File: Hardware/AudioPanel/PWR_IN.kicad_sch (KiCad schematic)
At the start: 30 parts, among them Q5 Q_PMOS, U17 LM358, U40 LM1084-ADJ, U41 NE5534

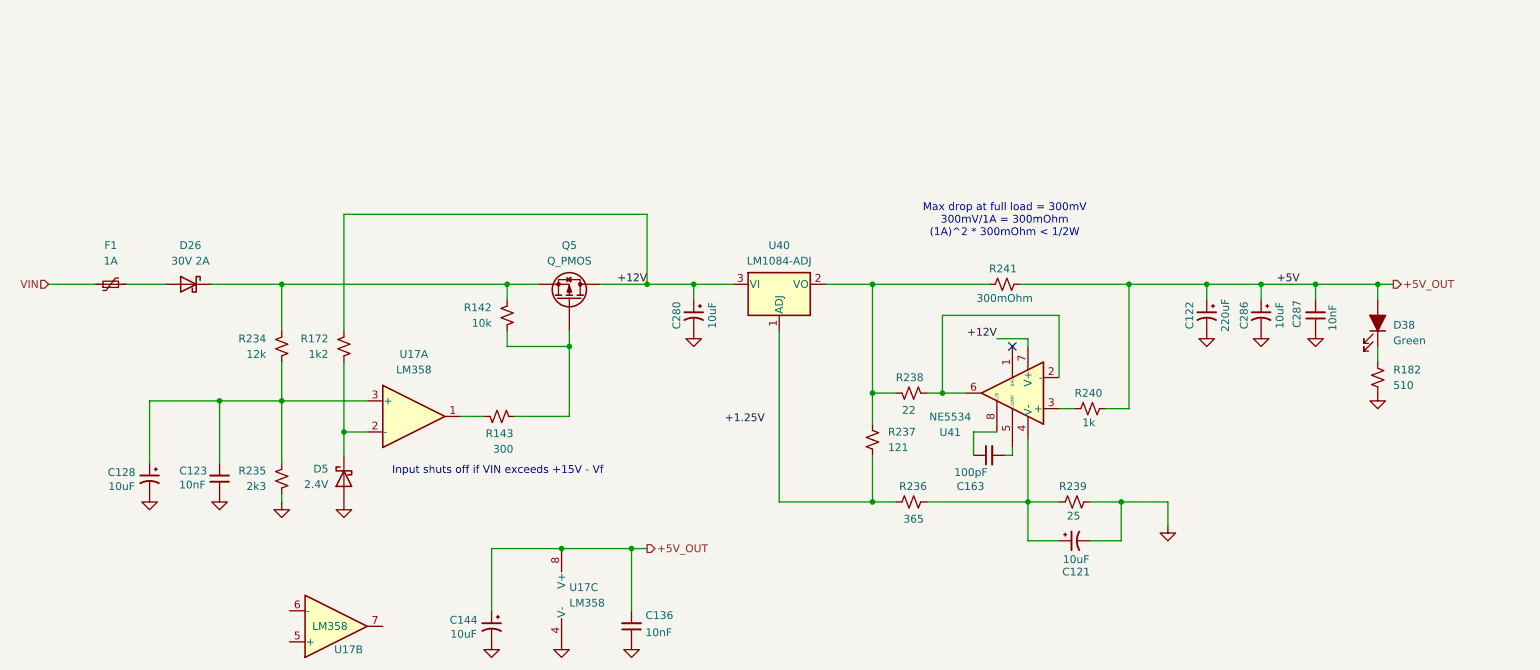
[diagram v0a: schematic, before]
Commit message: Added ideal diode controller to main power input
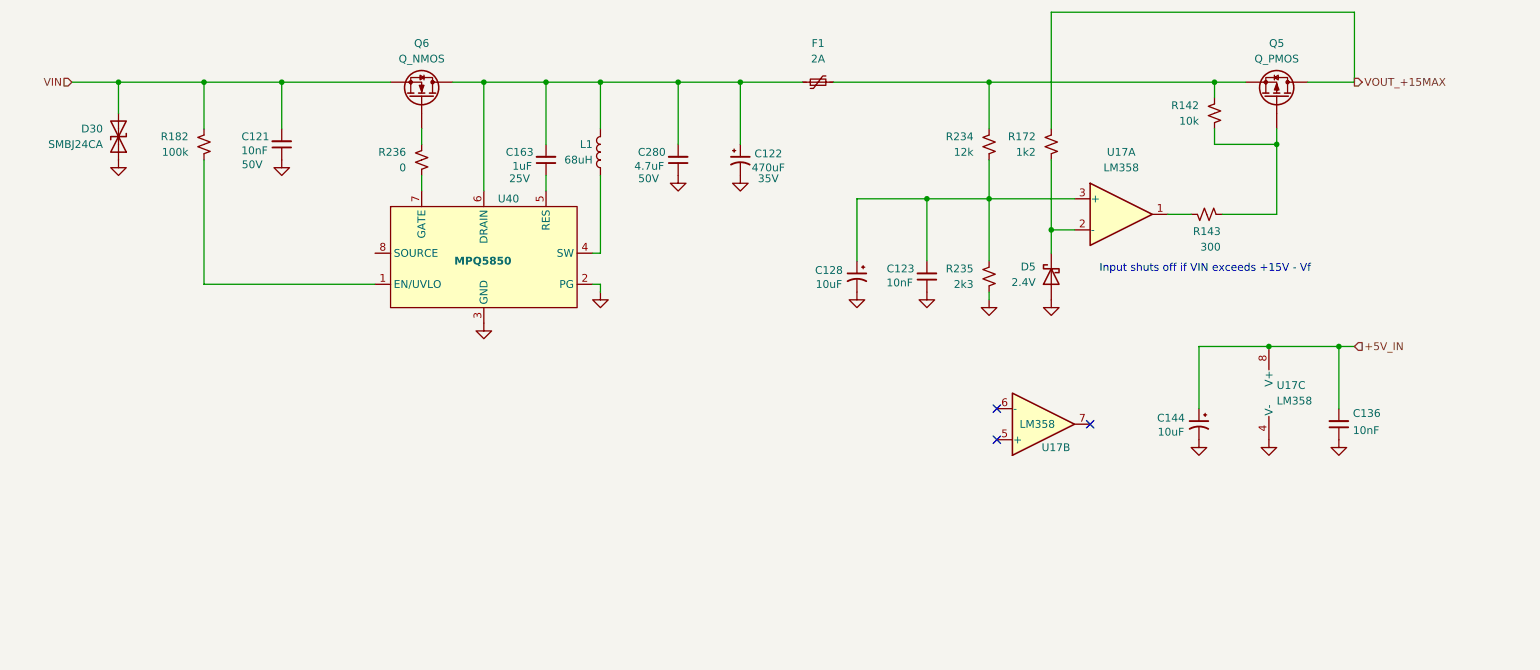
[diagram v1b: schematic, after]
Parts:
- removed C121, C280, C286: 10uF, symbol Device:C_Polarized_Small_US
- removed C287: 10nF, symbol Device:C_Small
- removed D26: 30V 2A, symbol Device:D_Schottky
- removed D38: Green, LED_THT:LED_D5.0mm, symbol Device:LED_Filled
- removed R237: 121, Resistor_SMD:R_0603_1608Metric_Pad0.98x0.95mm_HandSolder, symbol Device:R_Small_US
- removed R238: 22, Resistor_SMD:R_0603_1608Metric_Pad0.98x0.95mm_HandSolder, symbol Device:R_Small_US
- removed R239: 25, Resistor_SMD:R_0603_1608Metric_Pad0.98x0.95mm_HandSolder, symbol Device:R_Small_US
- removed R240: 1k, Resistor_SMD:R_0603_1608Metric_Pad0.98x0.95mm_HandSolder, symbol Device:R_Small_US
- removed R241: 300mOhm, Resistor_SMD:R_0603_1608Metric_Pad0.98x0.95mm_HandSolder, symbol Device:R_Small_US
- removed U40: LM1084-ADJ, symbol Regulator_Linear:LM1084-ADJ
- removed U41: NE5534, symbol Amplifier_Operational:NE5534
- added C121: 10nF, Capacitor_SMD:C_0603_1608Metric, symbol Device:C_Small
- added C280: 4.7uF, symbol Device:C_Small
- added D30: SMBJ24CA, symbol Device:D_TVS
- added L1: 68uH, symbol Device:L
- added Q6: Q_NMOS, symbol Device:Q_NMOS
- added U40: MPQ5850, Package_TO_SOT_SMD:TSOT-23-8, symbol AudioPanelLibrary:MPQ5850
- C122: value 220uF -> 470uF; Voltage (none) -> 35V
- C163: value 100pF -> 1uF; footprint (none) -> Capacitor_SMD:C_0805_2012Metric; Voltage (none) -> 25V
- F1: value 1A -> 2A
- R182: value 510 -> 100k
- R236: value 365 -> 0
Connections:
- net GND: now also C121.1, C280.1, D30.1 (A1), U40.2 (PG), U40.3 (GND); no longer R182.1
- net VIN: now also R182.2, C121.2, D30.2 (A2), Q6.S; no longer F1.1
- net at Q5.S, R142.2, R234.2: now also F1.2
- net at R236.1: now also U40.7 (GATE)
- net at R236.2: now also Q6.G
- net at C163.1: now also U40.5 (RES)
- net at C163.2: now also C122.1, F1.1, C280.2, L1.1, Q6.D, U40.6 (DRAIN)
- net +12V renamed VOUT_+15MAX
- net +5V_OUT renamed +5V_IN
- net +5V_IN: no longer C122.1
- new net: L1.2, U40.4 (SW)
- new net: R182.1, U40.1 (EN/UVLO)
- no-connect marks 1 -> 3
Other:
- note removed: "Max drop at full load = 300mV 300mV/1A = 300mOhm (1A)^2 * 300mOhm < 1/2W"
- moved on the sheet: C123, C128, C136, C144, D5, F1, Q5, R142, R143, R172, R234, R235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

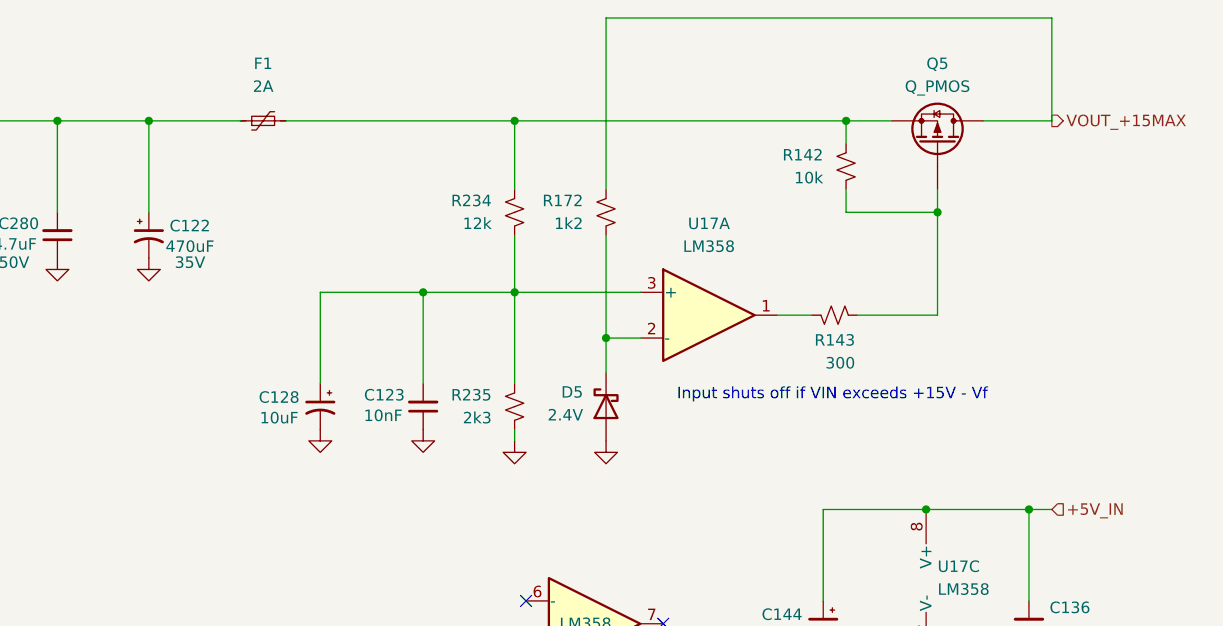
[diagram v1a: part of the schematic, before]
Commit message: Adding ADAV400 sheet
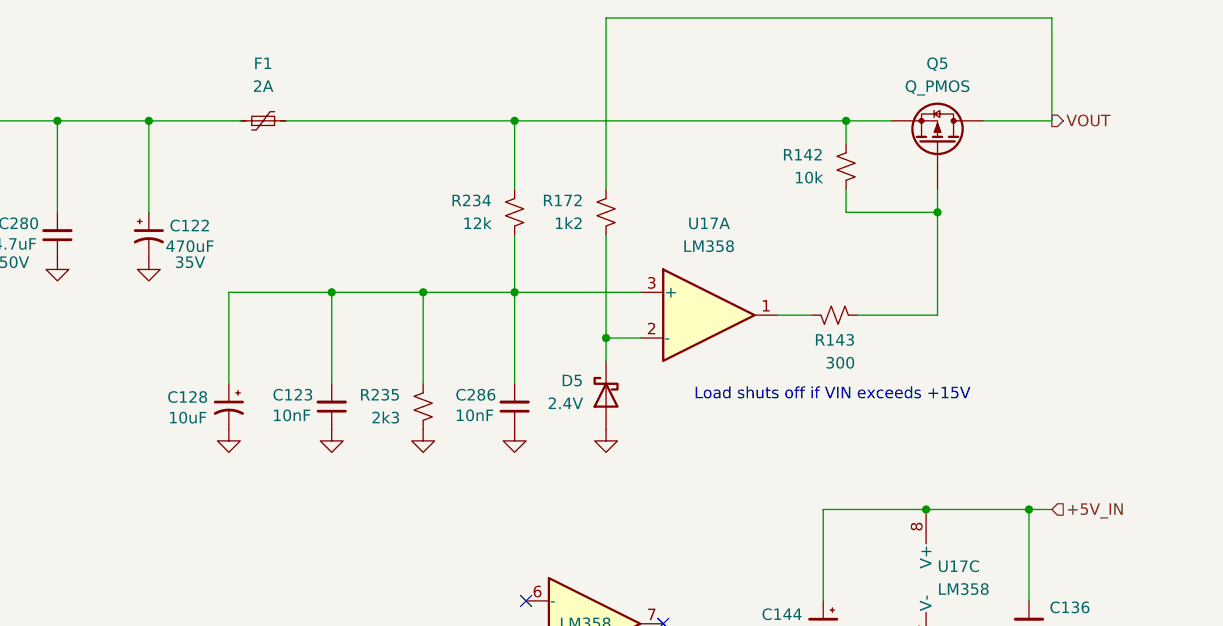
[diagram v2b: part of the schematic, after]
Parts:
- added C286: 10nF, symbol Device:C_Small
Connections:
- net GND: now also C286.1
- net at C123.2, C128.1, R234.1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: now also C286.2
- net VOUT_+15MAX renamed VOUT
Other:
- note added: "Load shuts off if VIN exceeds +15V"
- note removed: "Input shuts off if VIN exceeds +15V - Vf"
- moved on the sheet: C123, C128, D5, R235

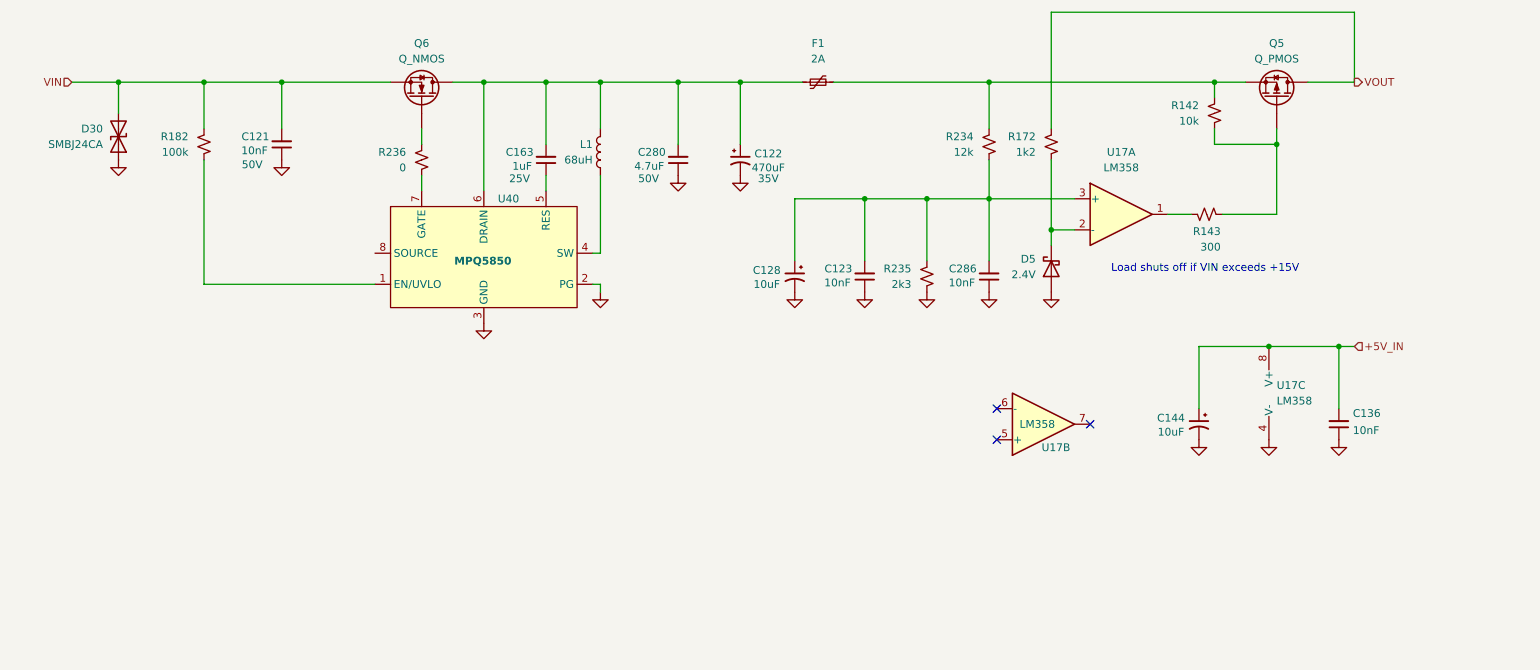
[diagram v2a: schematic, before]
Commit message: Realized that I need to rethink how I'm going to mix the radio audio with the stereo audio
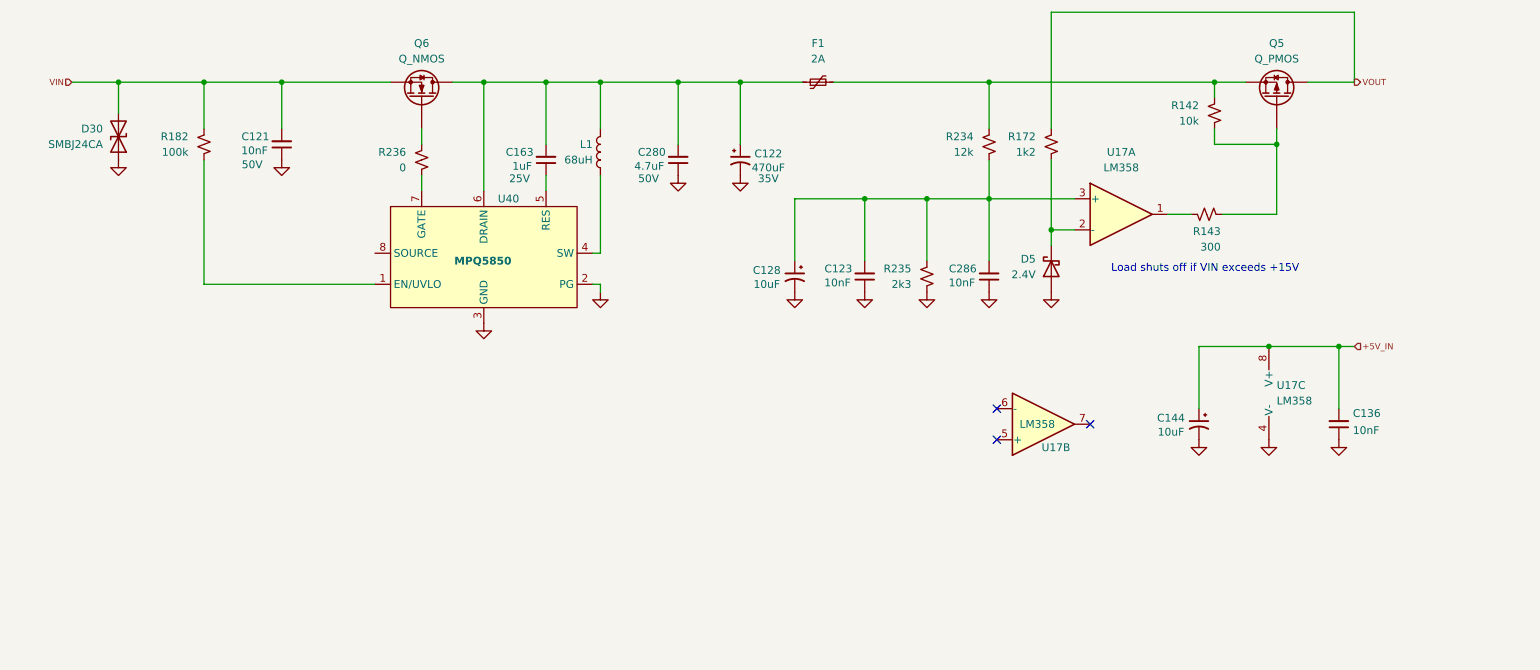
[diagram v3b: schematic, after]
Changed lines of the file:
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@@
 		(effects
 			(font
-				(size 1.27 1.27)
+				(size 1 1)
 			)
 			(justify left)
@@
 		(effects
 			(font
-				(size 1.27 1.27)
+				(size 1 1)
 			)
 			(justify left)
@@
 		(effects
 			(font
-				(size 1.27 1.27)
+				(size 1 1)
 			)
 			(justify right)

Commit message: Cleaned up stuff, defined more busses
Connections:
- net +5V_IN is gone; now on net VIN_PROTECTED: C136.2, C144.1, U17.8 (V+)
- net VIN: now also U40.8 (SOURCE)
- net VIN_PROTECTED: now reaches C122.1, C163.2, C280.2, F1.1, L1.1, Q6.D, U40.6 (DRAIN)
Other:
- note added: "Consider raising this threshold, maybe 18V?"
- moved on the sheet: F1
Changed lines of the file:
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@@
+		)
+	)
+	(text "Consider raising this threshold, maybe 18V?"
+		(exclude_from_sim no)
+		(at 245.872 101.854 0)
+		(effects
+			(font
+				(size 1.27 1.27)
+			)
 		)
 	)
@@
 	)
 	(junction
+		(at 241.3 119.38)
+		(diameter 0)
+		(color 0 0 0 0)
+	)
+	(junction
 		(at 163.83 95.25)
 		(diameter 0)
@@
 	)
 	(junction
+		(at 76.2 76.2)
+		(diameter 0)
+		(color 0 0 0 0)
+	)
+	(junction
 		(at 231.14 86.36)
 		(diameter 0)
@@
 		(color 0 0 0 0)
 	)
-	(junction
-		(at 241.3 119.38)
-		(diameter 0)
-		(color 0 0 0 0)
-	)
 	(no_connect
 		(at 200.66 132.08)
@@
 	(wire
 		(pts
+			(xy 83.82 104.14) (xy 76.2 104.14)
+		)
+		(stroke
+			(width 0)
+			(type default)
+		)
+	)
+	(wire
+		(pts
 			(xy 91.44 83.82) (xy 91.44 86.36)
 		)
@@
 	(wire
 		(pts
-			(xy 241.3 119.38) (xy 243.84 119.38)
-		)
-		(stroke
-			(width 0)
-			(type default)
-		)
-	)
-	(wire
-		(pts
 			(xy 119.38 104.14) (xy 120.65 104.14)
 		)
@@
 	(wire
 		(pts
-			(xy 68.58 76.2) (xy 86.36 76.2)
+			(xy 68.58 76.2) (xy 76.2 76.2)
 		)
 		(stroke
@@
 	(wire
 		(pts
+			(xy 76.2 76.2) (xy 76.2 104.14)
+		)
+		(stroke
+			(width 0)
+			(type default)
+		)
+	)
+	(wire
+		(pts
 			(xy 236.22 76.2) (xy 243.84 76.2)
 		)
@@
 	(wire
 		(pts
-			(xy 241.3 119.38) (xy 229.87 119.38)
+			(xy 257.81 119.38) (xy 241.3 119.38)
 		)
 		(stroke
@@
 	(wire
 		(pts
-			(xy 143.51 76.2) (xy 153.67 76.2)
+			(xy 143.51 76.2) (xy 166.37 76.2)
+		)
+		(stroke
+			(width 0)
+			(type default)
+		)
+	)
+	(wire
+		(pts
+			(xy 229.87 119.38) (xy 241.3 119.38)
+		)
+		(stroke
+			(width 0)
+			(type default)
+		)
+	)
+	(wire
+		(pts
+			(xy 76.2 76.2) (xy 86.36 76.2)
 		)
 		(stroke
@@
 	(wire
 		(pts
-			(xy 158.75 76.2) (xy 184.15 76.2)
+			(xy 171.45 76.2) (xy 184.15 76.2)
 		)
 		(stroke
@@
 		)
 	)
-	(hierarchical_label "+5V_IN"
-		(shape input)
-		(at 243.84 119.38 0)
+	(label "VIN_PROTECTED"
+		(at 146.05 76.2 0)
 		(effects
 			(font
-				(size 1 1)
-			)
-			(justify left)
+				(size 1.27 1.27)
+			)
+			(justify left bottom)
+		)
+	)
+	(label "VIN_PROTECTED"
+		(at 257.81 119.38 180)
+		(effects
+			(font
+				(size 1.27 1.27)
+			)
+			(justify right bottom)
 		)
 	)
@@
 	(symbol
 		(lib_id "Device:Polyfuse_Small")
-		(at 156.21 76.2 90)
+		(at 168.91 76.2 90)
 		(unit 1)
 		(exclude_from_sim no)
@@
 		(fields_autoplaced yes)
 		(property "Reference" "F1"
-			(at 156.21 69.85 90)
+			(at 168.91 69.85 90)
 			(effects
 				(font
@@
 		)
 		(property "Value" "2A"
-			(at 156.21 72.39 90)
+			(at 168.91 72.39 90)
 			(effects
 				(font
@@
 		)
 		(property "Footprint" ""
-			(at 161.29 74.93 0)
+			(at 173.99 74.93 0)
 			(effects
 				(font
@@
 		)
 		(property "Datasheet" "~"
-			(at 156.21 76.2 0)
+			(at 168.91 76.2 0)
 			(effects
 				(font
@@
 		)
 		(property "Description" "Resettable fuse, polymeric positive temperature coefficient, small symbol"
-			(at 156.21 76.2 0)
-			(effects
-				(font
+			(at 168.91 76.2 0)
+			(effects
+				(font
